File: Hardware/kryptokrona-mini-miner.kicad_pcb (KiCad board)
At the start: 4 copper layers, 26.5 x 86.9 mm, 111 parts, among them J1 Micro_SD_Card_Det2, J2 USB_C_Receptacle_USB2.0, J3 USB_A, U1 H616, U2 DDR3 FBGA-96, U4 CP2102N-Axx-xQFN28, Y1 25MHz

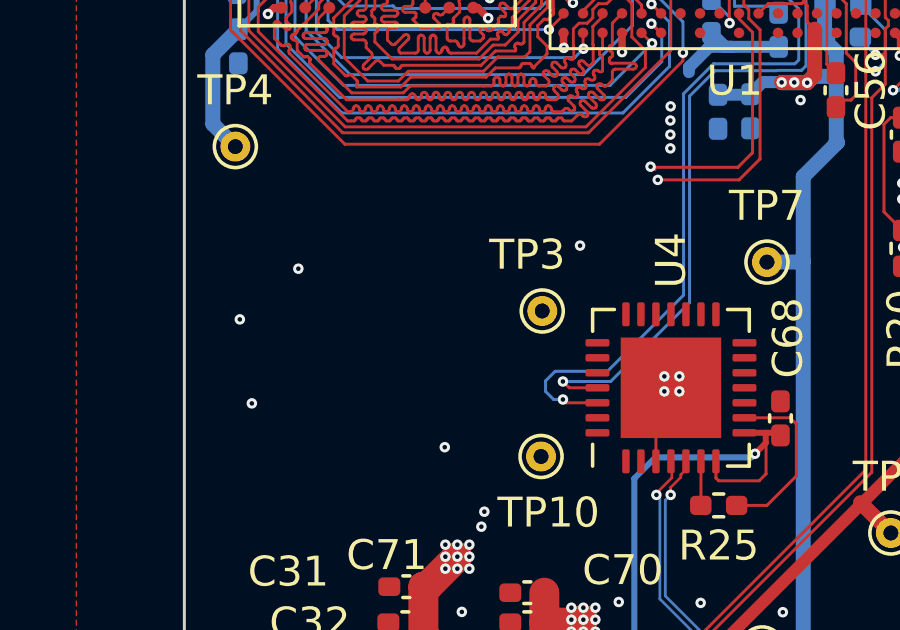
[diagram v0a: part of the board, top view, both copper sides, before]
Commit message: added testpoint for TX/RX and updated readme
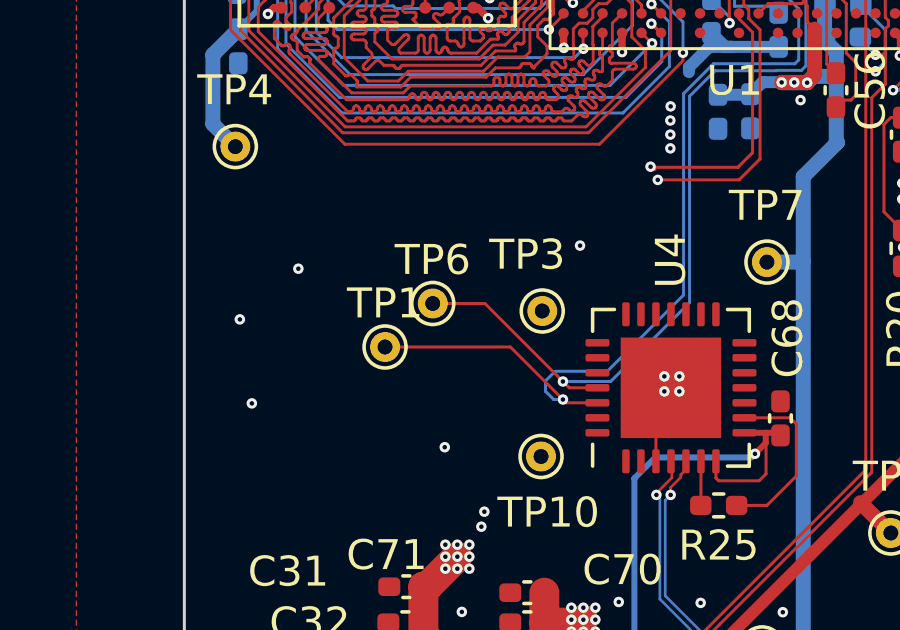
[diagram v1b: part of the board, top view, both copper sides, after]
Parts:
- added TP1: TestPoint, TestPoint:TestPoint_THTPad_D1.0mm_Drill0.5mm, F.Cu at (134.6, 107.3)
- added TP6: TestPoint, TestPoint:TestPoint_THTPad_D1.0mm_Drill0.5mm, F.Cu at (136.2, 105.9)
- Y1: value 25MHz -> 24MHz
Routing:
- net TXConvOut: track 28.6 -> 35.2 mm
- net RXConvIn: track 24.0 -> 29.4 mm
